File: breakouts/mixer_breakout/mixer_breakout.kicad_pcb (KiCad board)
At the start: 4 copper layers, 26.8 x 26.5 mm, 13 parts, among them P1 CONN_01X04, U1 CONN_SMA, U2 LTC5549, U3 CONN_SMA, U4 CONN_SMA

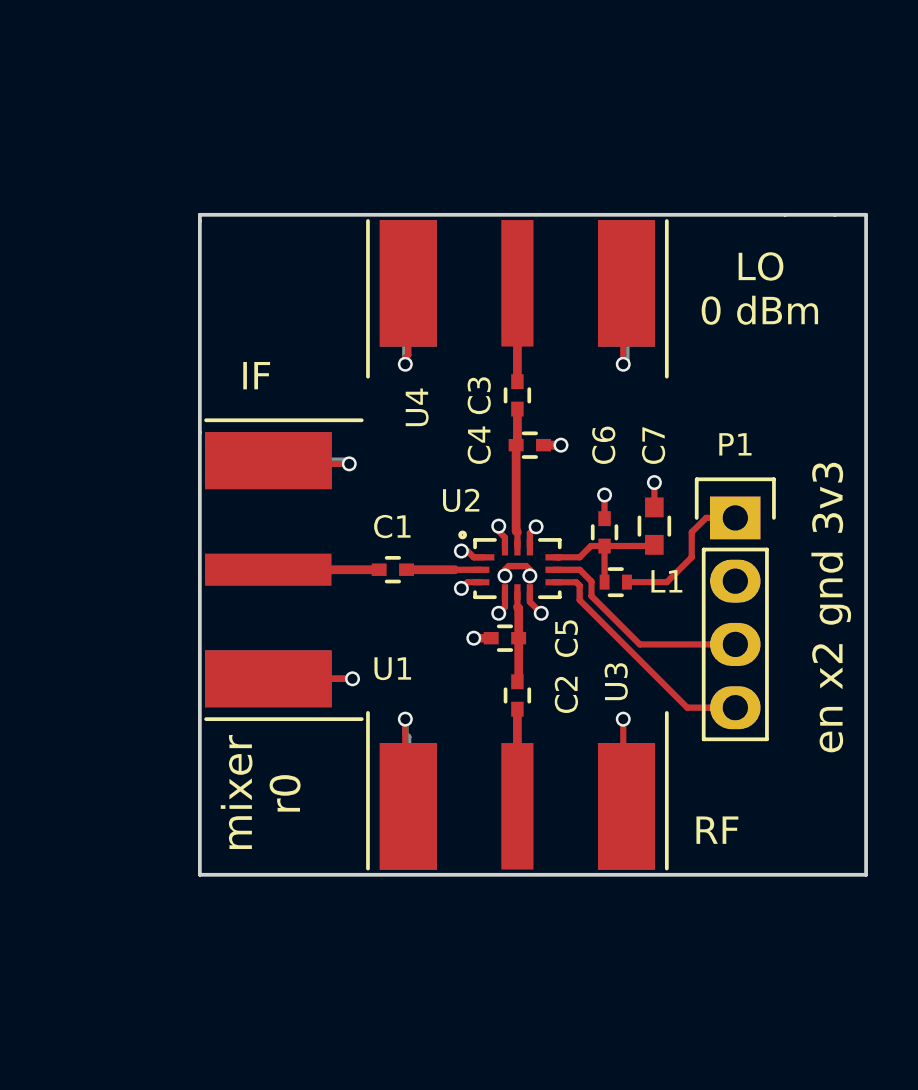
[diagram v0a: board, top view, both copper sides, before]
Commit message: finished bias module, modified mixer, splitter, and switch sma connector footprints
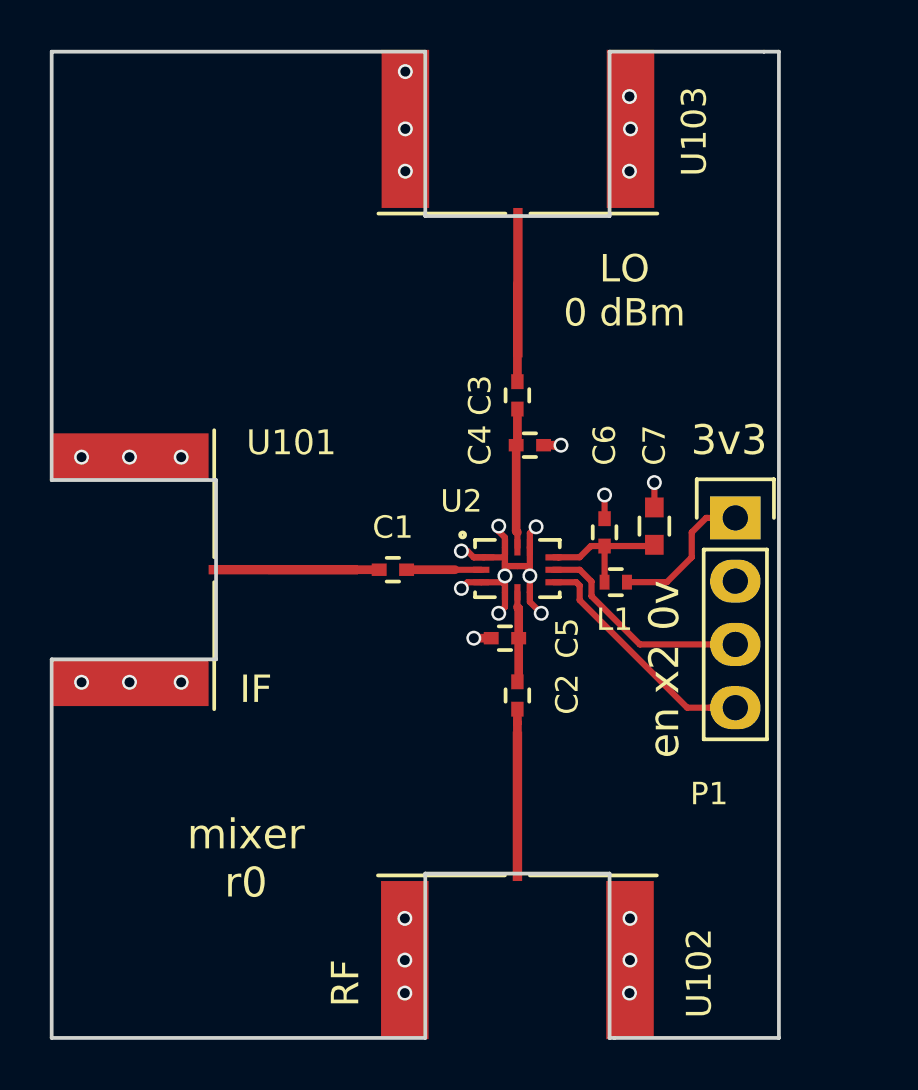
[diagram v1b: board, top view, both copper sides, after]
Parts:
- removed U1, U3, U4: CONN_SMA, vna_footprints:732511150_sma_thin
- added U101: CONN_SMA_2GND, vna_footprints:142-0721-882_sma_cutout, F.Cu at (132.9, 105.0)
- added U102: CONN_SMA_2GND, vna_footprints:142-0721-882_sma_cutout, F.Cu at (148.5, 120.7)
- added U103: CONN_SMA_2GND, vna_footprints:142-0721-882_sma_cutout, F.Cu at (148.5, 87.3)
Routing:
- net GND: track 48.0 -> 16.5 mm, vias 18 -> 30
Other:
- board size 26.8 x 26.5 mm -> 29.2 x 39.6 mm
- net class Default: clearance 0.2 -> 0.127
- rule trace_clearance: 0.2 -> 0.127
- rule trace_min: 0.2 -> 0.127
- board text added: "3v3"
- board text added: "en x2 0v"
- board text removed: "en x2 gnd 3v3"

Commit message: ordered r1 synth board, ordered coplanar waveguide mixer breakout
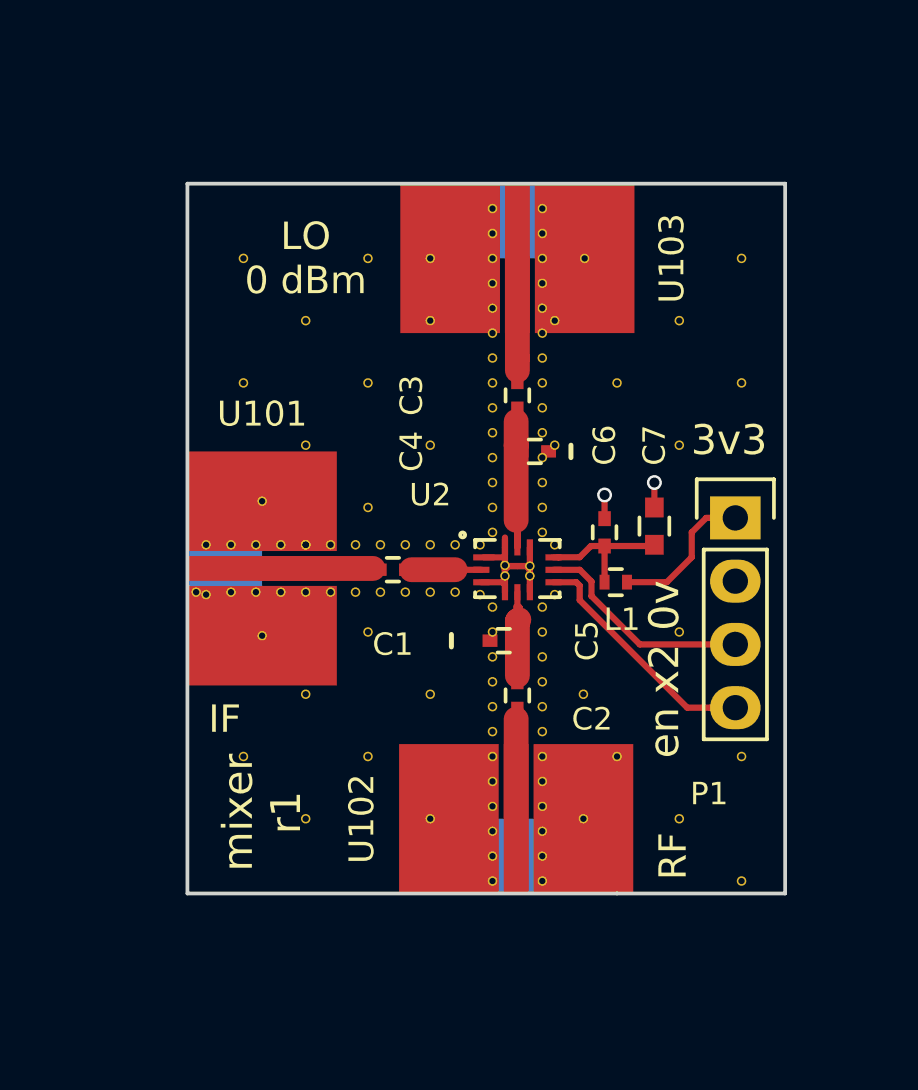
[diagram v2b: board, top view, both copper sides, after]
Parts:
- added REF**: VIA_OSH4LAYER_MIN, vna_footprints:VIA_OSH4LAYER_MIN, F.Cu at (138.2, 107.7)
- added REF**: VIA_OSH4LAYER_MIN, vna_footprints:VIA_OSH4LAYER_MIN, F.Cu at (142.5, 102.5)
- added REF** (x2): VIA_OSH4LAYER_MIN, vna_footprints:VIA_OSH4LAYER_MIN, F.Cu at (140.0, 104.0)
- added REF**: VIA_OSH4LAYER_MIN, vna_footprints:VIA_OSH4LAYER_MIN, F.Cu at (141.0, 104.0)
- added REF**: VIA_OSH4LAYER_MIN, vna_footprints:VIA_OSH4LAYER_MIN, F.Cu at (142.0, 104.0)
- added REF**: VIA_OSH4LAYER_MIN, vna_footprints:VIA_OSH4LAYER_MIN, F.Cu at (144.0, 104.0)
- added REF**: VIA_OSH4LAYER_MIN, vna_footprints:VIA_OSH4LAYER_MIN, F.Cu at (143.0, 104.0)
- added REF**: VIA_OSH4LAYER_MIN, vna_footprints:VIA_OSH4LAYER_MIN, F.Cu at (145.0, 104.0)
- added REF**: VIA_OSH4LAYER_MIN, vna_footprints:VIA_OSH4LAYER_MIN, F.Cu at (146.0, 104.0)
- added REF**: VIA_OSH4LAYER_MIN, vna_footprints:VIA_OSH4LAYER_MIN, F.Cu at (146.0, 105.9)
- added REF**: VIA_OSH4LAYER_MIN, vna_footprints:VIA_OSH4LAYER_MIN, F.Cu at (145.0, 105.9)
- added REF**: VIA_OSH4LAYER_MIN, vna_footprints:VIA_OSH4LAYER_MIN, F.Cu at (142.5, 107.5)
- added REF**: VIA_OSH4LAYER_MIN, vna_footprints:VIA_OSH4LAYER_MIN, F.Cu at (144.0, 105.9)
- added REF**: VIA_OSH4LAYER_MIN, vna_footprints:VIA_OSH4LAYER_MIN, F.Cu at (143.0, 105.9)
- added REF**: VIA_OSH4LAYER_MIN, vna_footprints:VIA_OSH4LAYER_MIN, F.Cu at (142.0, 105.9)
- added REF**: VIA_OSH4LAYER_MIN, vna_footprints:VIA_OSH4LAYER_MIN, F.Cu at (141.0, 105.9)
- added REF**: VIA_OSH4LAYER_MIN, vna_footprints:VIA_OSH4LAYER_MIN, F.Cu at (140.0, 105.9)
- added REF**: VIA_OSH4LAYER_MIN, vna_footprints:VIA_OSH4LAYER_MIN, F.Cu at (139.0, 105.9)
- added REF**: VIA_OSH4LAYER_MIN, vna_footprints:VIA_OSH4LAYER_MIN, F.Cu at (138.0, 105.9)
- added REF**: VIA_OSH4LAYER_MIN, vna_footprints:VIA_OSH4LAYER_MIN, F.Cu at (137.0, 105.9)
- added REF**: VIA_OSH4LAYER_MIN, vna_footprints:VIA_OSH4LAYER_MIN, F.Cu at (135.6, 105.9)
- added REF**: VIA_OSH4LAYER_MIN, vna_footprints:VIA_OSH4LAYER_MIN, F.Cu at (137.5, 112.5)
- added REF**: VIA_OSH4LAYER_MIN, vna_footprints:VIA_OSH4LAYER_MIN, F.Cu at (142.5, 112.5)
- added REF**: VIA_OSH4LAYER_MIN, vna_footprints:VIA_OSH4LAYER_MIN, F.Cu at (152.5, 112.5)
- added REF**: VIA_OSH4LAYER_MIN, vna_footprints:VIA_OSH4LAYER_MIN, F.Cu at (157.5, 112.5)
- added REF**: VIA_OSH4LAYER_MIN, vna_footprints:VIA_OSH4LAYER_MIN, F.Cu at (157.5, 97.5)
- added REF**: VIA_OSH4LAYER_MIN, vna_footprints:VIA_OSH4LAYER_MIN, F.Cu at (152.5, 97.5)
- added REF**: VIA_OSH4LAYER_MIN, vna_footprints:VIA_OSH4LAYER_MIN, F.Cu at (137.5, 97.5)
- added REF**: VIA_OSH4LAYER_MIN, vna_footprints:VIA_OSH4LAYER_MIN, F.Cu at (142.5, 97.5)
- added REF**: VIA_OSH4LAYER_MIN, vna_footprints:VIA_OSH4LAYER_MIN, F.Cu at (145.0, 92.5)
- added REF**: VIA_OSH4LAYER_MIN, vna_footprints:VIA_OSH4LAYER_MIN, F.Cu at (145.0, 100.0)
- added REF**: VIA_OSH4LAYER_MIN, vna_footprints:VIA_OSH4LAYER_MIN, F.Cu at (140.0, 100.0)
- added REF**: VIA_OSH4LAYER_MIN, vna_footprints:VIA_OSH4LAYER_MIN, F.Cu at (140.0, 95.0)
- added REF**: VIA_OSH4LAYER_MIN, vna_footprints:VIA_OSH4LAYER_MIN, F.Cu at (145.0, 95.0)
- added REF**: VIA_OSH4LAYER_MIN, vna_footprints:VIA_OSH4LAYER_MIN, F.Cu at (155.0, 95.0)
- added REF**: VIA_OSH4LAYER_MIN, vna_footprints:VIA_OSH4LAYER_MIN, F.Cu at (150.0, 95.0)
- added REF**: VIA_OSH4LAYER_MIN, vna_footprints:VIA_OSH4LAYER_MIN, F.Cu at (150.0, 100.0)
- added REF**: VIA_OSH4LAYER_MIN, vna_footprints:VIA_OSH4LAYER_MIN, F.Cu at (155.0, 100.0)
- added REF**: VIA_OSH4LAYER_MIN, vna_footprints:VIA_OSH4LAYER_MIN, F.Cu at (155.0, 115.0)
- added REF**: VIA_OSH4LAYER_MIN, vna_footprints:VIA_OSH4LAYER_MIN, F.Cu at (151.2, 110.0)
- added REF**: VIA_OSH4LAYER_MIN, vna_footprints:VIA_OSH4LAYER_MIN, F.Cu at (137.5, 92.5)
- added REF**: VIA_OSH4LAYER_MIN, vna_footprints:VIA_OSH4LAYER_MIN, F.Cu at (151.2, 115.0)
- added REF**: VIA_OSH4LAYER_MIN, vna_footprints:VIA_OSH4LAYER_MIN, F.Cu at (145.0, 115.0)
- added REF**: VIA_OSH4LAYER_MIN, vna_footprints:VIA_OSH4LAYER_MIN, F.Cu at (140.0, 115.0)
- added REF**: VIA_OSH4LAYER_MIN, vna_footprints:VIA_OSH4LAYER_MIN, F.Cu at (140.0, 110.0)
- added REF**: VIA_OSH4LAYER_MIN, vna_footprints:VIA_OSH4LAYER_MIN, F.Cu at (145.0, 110.0)
- added REF**: VIA_OSH4LAYER_MIN, vna_footprints:VIA_OSH4LAYER_MIN, F.Cu at (147.5, 106.5)
- added REF**: VIA_OSH4LAYER_MIN, vna_footprints:VIA_OSH4LAYER_MIN, F.Cu at (147.5, 107.5)
- added REF**: VIA_OSH4LAYER_MIN, vna_footprints:VIA_OSH4LAYER_MIN, F.Cu at (147.5, 108.5)
- added REF**: VIA_OSH4LAYER_MIN, vna_footprints:VIA_OSH4LAYER_MIN, F.Cu at (147.5, 109.5)
- added REF**: VIA_OSH4LAYER_MIN, vna_footprints:VIA_OSH4LAYER_MIN, F.Cu at (147.5, 110.5)
- added REF**: VIA_OSH4LAYER_MIN, vna_footprints:VIA_OSH4LAYER_MIN, F.Cu at (142.5, 92.5)
- added REF**: VIA_OSH4LAYER_MIN, vna_footprints:VIA_OSH4LAYER_MIN, F.Cu at (147.5, 111.5)
- added REF**: VIA_OSH4LAYER_MIN, vna_footprints:VIA_OSH4LAYER_MIN, F.Cu at (147.5, 112.5)
- added REF**: VIA_OSH4LAYER_MIN, vna_footprints:VIA_OSH4LAYER_MIN, F.Cu at (147.5, 113.5)
- added REF**: VIA_OSH4LAYER_MIN, vna_footprints:VIA_OSH4LAYER_MIN, F.Cu at (147.5, 114.5)
- added REF**: VIA_OSH4LAYER_MIN, vna_footprints:VIA_OSH4LAYER_MIN, F.Cu at (147.5, 115.5)
- added REF**: VIA_OSH4LAYER_MIN, vna_footprints:VIA_OSH4LAYER_MIN, F.Cu at (147.5, 116.5)
- added REF**: VIA_OSH4LAYER_MIN, vna_footprints:VIA_OSH4LAYER_MIN, F.Cu at (147.5, 117.5)
- added REF**: VIA_OSH4LAYER_MIN, vna_footprints:VIA_OSH4LAYER_MIN, F.Cu at (149.5, 117.5)
- added REF**: VIA_OSH4LAYER_MIN, vna_footprints:VIA_OSH4LAYER_MIN, F.Cu at (149.5, 116.5)
- added REF**: VIA_OSH4LAYER_MIN, vna_footprints:VIA_OSH4LAYER_MIN, F.Cu at (149.5, 115.5)
- added REF**: VIA_OSH4LAYER_MIN, vna_footprints:VIA_OSH4LAYER_MIN, F.Cu at (151.2, 92.5)
- added REF**: VIA_OSH4LAYER_MIN, vna_footprints:VIA_OSH4LAYER_MIN, F.Cu at (149.5, 114.5)
- added REF**: VIA_OSH4LAYER_MIN, vna_footprints:VIA_OSH4LAYER_MIN, F.Cu at (149.5, 113.5)
- added REF**: VIA_OSH4LAYER_MIN, vna_footprints:VIA_OSH4LAYER_MIN, F.Cu at (149.5, 112.5)
- added REF**: VIA_OSH4LAYER_MIN, vna_footprints:VIA_OSH4LAYER_MIN, F.Cu at (149.5, 111.5)
- added REF**: VIA_OSH4LAYER_MIN, vna_footprints:VIA_OSH4LAYER_MIN, F.Cu at (149.5, 110.5)
- added REF**: VIA_OSH4LAYER_MIN, vna_footprints:VIA_OSH4LAYER_MIN, F.Cu at (149.5, 109.5)
- added REF**: VIA_OSH4LAYER_MIN, vna_footprints:VIA_OSH4LAYER_MIN, F.Cu at (149.5, 108.5)
- added REF**: VIA_OSH4LAYER_MIN, vna_footprints:VIA_OSH4LAYER_MIN, F.Cu at (149.5, 107.5)
- added REF**: VIA_OSH4LAYER_MIN, vna_footprints:VIA_OSH4LAYER_MIN, F.Cu at (149.5, 106.5)
- added REF**: VIA_OSH4LAYER_MIN, vna_footprints:VIA_OSH4LAYER_MIN, F.Cu at (147.5, 103.5)
- added REF**: VIA_OSH4LAYER_MIN, vna_footprints:VIA_OSH4LAYER_MIN, F.Cu at (157.5, 92.5)
- added REF**: VIA_OSH4LAYER_MIN, vna_footprints:VIA_OSH4LAYER_MIN, F.Cu at (147.5, 102.5)
- added REF**: VIA_OSH4LAYER_MIN, vna_footprints:VIA_OSH4LAYER_MIN, F.Cu at (147.5, 101.5)
- added REF**: VIA_OSH4LAYER_MIN, vna_footprints:VIA_OSH4LAYER_MIN, F.Cu at (147.5, 100.5)
- added REF**: VIA_OSH4LAYER_MIN, vna_footprints:VIA_OSH4LAYER_MIN, F.Cu at (147.5, 99.5)
- added REF**: VIA_OSH4LAYER_MIN, vna_footprints:VIA_OSH4LAYER_MIN, F.Cu at (147.5, 98.5)
- added REF**: VIA_OSH4LAYER_MIN, vna_footprints:VIA_OSH4LAYER_MIN, F.Cu at (147.5, 97.5)
- added REF**: VIA_OSH4LAYER_MIN, vna_footprints:VIA_OSH4LAYER_MIN, F.Cu at (147.5, 96.5)
- added REF**: VIA_OSH4LAYER_MIN, vna_footprints:VIA_OSH4LAYER_MIN, F.Cu at (147.5, 95.5)
- added REF**: VIA_OSH4LAYER_MIN, vna_footprints:VIA_OSH4LAYER_MIN, F.Cu at (147.5, 94.5)
- added REF**: VIA_OSH4LAYER_MIN, vna_footprints:VIA_OSH4LAYER_MIN, F.Cu at (147.5, 93.5)
- added REF**: VIA_OSH4LAYER_MIN, vna_footprints:VIA_OSH4LAYER_MIN, F.Cu at (157.5, 117.5)
- added REF**: VIA_OSH4LAYER_MIN, vna_footprints:VIA_OSH4LAYER_MIN, F.Cu at (147.5, 92.5)
- added REF**: VIA_OSH4LAYER_MIN, vna_footprints:VIA_OSH4LAYER_MIN, F.Cu at (147.5, 91.5)
- added REF**: VIA_OSH4LAYER_MIN, vna_footprints:VIA_OSH4LAYER_MIN, F.Cu at (147.5, 90.5)
- added REF**: VIA_OSH4LAYER_MIN, vna_footprints:VIA_OSH4LAYER_MIN, F.Cu at (149.5, 90.5)
- added REF**: VIA_OSH4LAYER_MIN, vna_footprints:VIA_OSH4LAYER_MIN, F.Cu at (149.5, 91.5)
- added REF**: VIA_OSH4LAYER_MIN, vna_footprints:VIA_OSH4LAYER_MIN, F.Cu at (149.5, 92.5)
- added REF**: VIA_OSH4LAYER_MIN, vna_footprints:VIA_OSH4LAYER_MIN, F.Cu at (149.5, 93.5)
- added REF**: VIA_OSH4LAYER_MIN, vna_footprints:VIA_OSH4LAYER_MIN, F.Cu at (149.5, 94.5)
- added REF**: VIA_OSH4LAYER_MIN, vna_footprints:VIA_OSH4LAYER_MIN, F.Cu at (149.5, 95.5)
- added REF**: VIA_OSH4LAYER_MIN, vna_footprints:VIA_OSH4LAYER_MIN, F.Cu at (149.5, 96.5)
- added REF**: VIA_OSH4LAYER_MIN, vna_footprints:VIA_OSH4LAYER_MIN, F.Cu at (155.0, 107.5)
- added REF**: VIA_OSH4LAYER_MIN, vna_footprints:VIA_OSH4LAYER_MIN, F.Cu at (149.5, 97.5)
- added REF**: VIA_OSH4LAYER_MIN, vna_footprints:VIA_OSH4LAYER_MIN, F.Cu at (149.5, 98.5)
- added REF**: VIA_OSH4LAYER_MIN, vna_footprints:VIA_OSH4LAYER_MIN, F.Cu at (149.5, 99.5)
- added REF**: VIA_OSH4LAYER_MIN, vna_footprints:VIA_OSH4LAYER_MIN, F.Cu at (149.5, 100.5)
- added REF**: VIA_OSH4LAYER_MIN, vna_footprints:VIA_OSH4LAYER_MIN, F.Cu at (149.5, 101.5)
- added REF**: VIA_OSH4LAYER_MIN, vna_footprints:VIA_OSH4LAYER_MIN, F.Cu at (149.5, 102.5)
- added REF**: VIA_OSH4LAYER_MIN, vna_footprints:VIA_OSH4LAYER_MIN, F.Cu at (149.5, 103.5)
- added REF**: VIA_OSH4LAYER_MIN, vna_footprints:VIA_OSH4LAYER_MIN, F.Cu at (147.0, 106.0)
- added REF**: VIA_OSH4LAYER_MIN, vna_footprints:VIA_OSH4LAYER_MIN, F.Cu at (150.0, 106.0)
- added REF**: VIA_OSH4LAYER_MIN, vna_footprints:VIA_OSH4LAYER_MIN, F.Cu at (150.0, 104.0)
- added REF**: VIA_OSH4LAYER_MIN, vna_footprints:VIA_OSH4LAYER_MIN, F.Cu at (138.2, 102.2)
- added REF**: VIA_OSH4LAYER_MIN, vna_footprints:VIA_OSH4LAYER_MIN, F.Cu at (147.0, 104.0)
- added REF**: VIA_OSH4LAYER_MIN, vna_footprints:VIA_OSH4LAYER_MIN, F.Cu at (149.0, 104.9)
- added REF**: VIA_OSH4LAYER_MIN, vna_footprints:VIA_OSH4LAYER_MIN, F.Cu at (149.0, 105.3)
- added REF**: VIA_OSH4LAYER_MIN, vna_footprints:VIA_OSH4LAYER_MIN, F.Cu at (148.0, 105.3)
- added REF**: VIA_OSH4LAYER_MIN, vna_footprints:VIA_OSH4LAYER_MIN, F.Cu at (148.0, 104.8)
- added REF**: VIA_OSH4LAYER_MIN, vna_footprints:VIA_OSH4LAYER_MIN, F.Cu at (136.0, 106.0)
- added REF**: VIA_OSH4LAYER_MIN, vna_footprints:VIA_OSH4LAYER_MIN, F.Cu at (136.0, 104.0)
- added REF**: VIA_OSH4LAYER_MIN, vna_footprints:VIA_OSH4LAYER_MIN, F.Cu at (137.0, 104.0)
- added REF**: VIA_OSH4LAYER_MIN, vna_footprints:VIA_OSH4LAYER_MIN, F.Cu at (138.0, 104.0)
- added REF**: VIA_OSH4LAYER_MIN, vna_footprints:VIA_OSH4LAYER_MIN, F.Cu at (139.0, 104.0)
- U101, U102, U103: footprint vna_footprints:142-0721-882_sma_cutout -> vna_footprints:SMA_CPW_1MM_.2MM
- moved U102 5.68 mm to (148.4, 115.0), turned to 180 degrees
- moved U101 5.33 mm to (138.2, 105.0), turned to 90 degrees
- moved U103 5.20 mm to (148.5, 92.5), turned to 0 degrees
- moved C4 0.32 mm to (149.2, 100.2)
- moved C5 0.11 mm to (147.9, 107.8)
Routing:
- net GND: track 16.5 -> 9.74 mm, vias 30 -> 2
- net Net-(C3-Pad1): track 3.95 -> 5.08 mm
- net Net-(C2-Pad2): track 3.64 -> 4.67 mm
- net Net-(C3-Pad2): track 5.60 -> 6.20 mm
- net Net-(C2-Pad1): track 3.90 -> 4.42 mm
- added copper zone on F.Cu, net GND
- added copper zone on In2.Cu, net GND
- removed copper zone on In1.Cu, net GND
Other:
- board size 29.2 x 39.6 mm -> 24 x 28.5 mm
- board text added: "mixer r1"
- board text removed: "mixer r0"
